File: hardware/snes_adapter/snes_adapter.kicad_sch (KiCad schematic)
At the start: 5 parts, among them J1 CART SLOT TOP ROW, J2 CART SLOT BOTTOM ROW, J3 SNES_Slot, U1 PIC12F629-IP

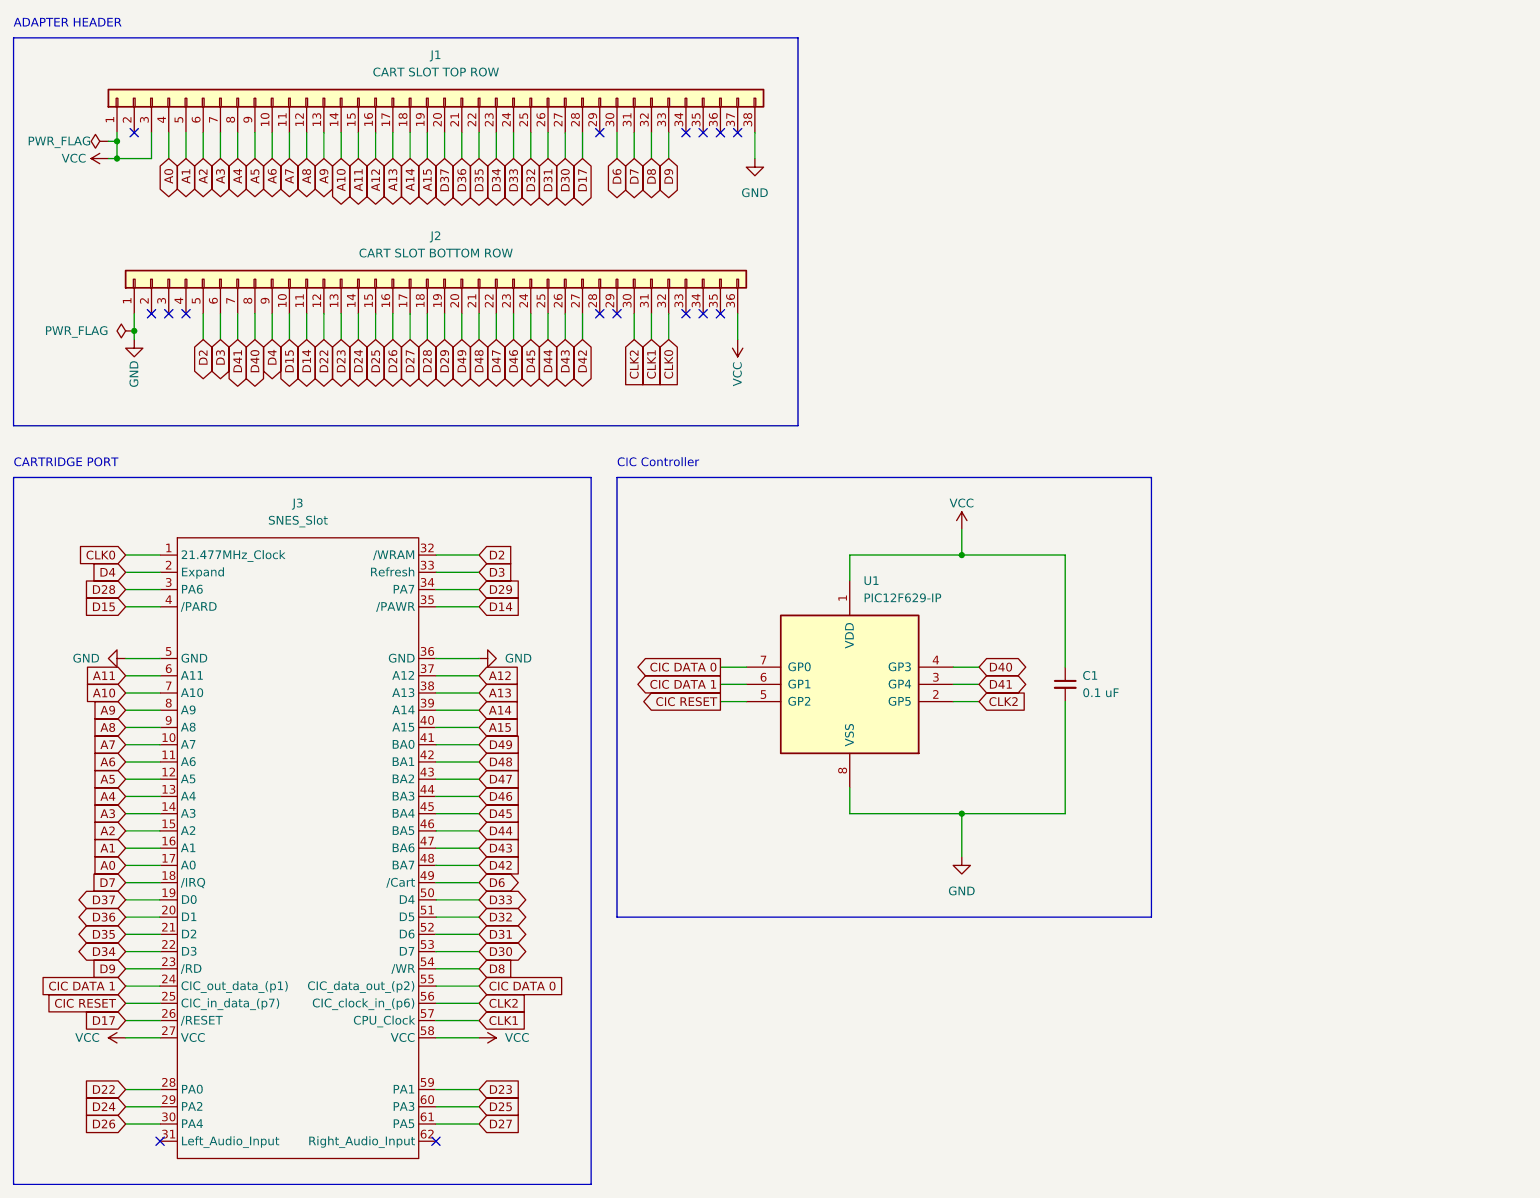
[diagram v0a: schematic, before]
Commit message: move SNES updates to clean branch
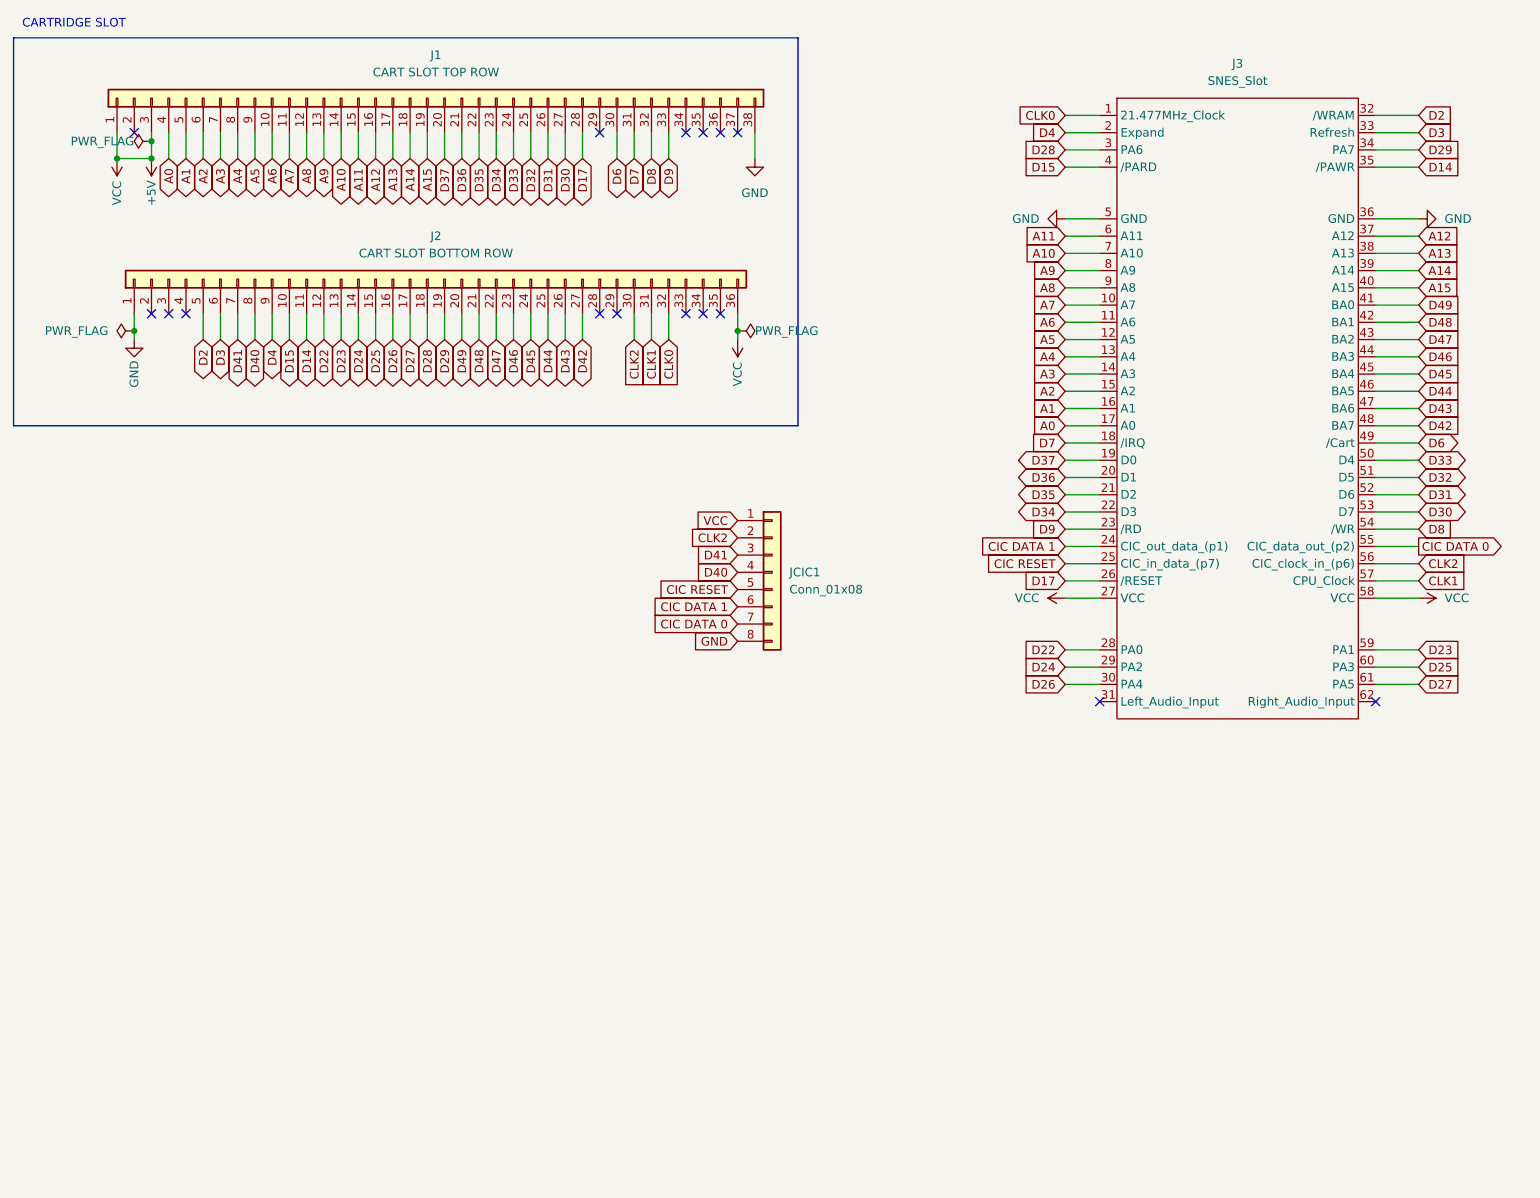
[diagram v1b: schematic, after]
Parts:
- removed C1: 0.1 uF, Capacitor_THT:C_Disc_D5.0mm_W2.5mm_P5.00mm, symbol Device:C_Small
- removed U1: PIC12F629-IP, Package_DIP:DIP-8_W7.62mm, symbol MCU_Microchip_PIC12:PIC12F629-IP
- added JCIC1: Conn_01x08, symbol Connector_Generic:Conn_01x08
- J1: footprint Connector_PinHeader_2.54mm:PinHeader_1x38_P2.54mm_Vertical -> Connector_PinSocket_2.54mm:PinSocket_1x38_P2.54mm_Vertical
- J2: footprint Connector_PinHeader_2.54mm:PinHeader_1x36_P2.54mm_Vertical -> Connector_PinSocket_2.54mm:PinSocket_1x36_P2.54mm_Vertical
- J3: footprint !OSCR:SNES Slot -> (none); symbol !OSCR:SNES_Slot -> sanni:SNES_Slot
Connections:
- net CIC DATA 0: now also JCIC1.7 (Pin_7)
- net CIC DATA 1: now also JCIC1.6 (Pin_6)
- net CIC RESET: now also JCIC1.5 (Pin_5)
- net CLK2: now also JCIC1.2 (Pin_2)
- net D40: now also JCIC1.4 (Pin_4)
- net D41: now also JCIC1.3 (Pin_3)
- net GND: now also JCIC1.8 (Pin_8)
- net VCC renamed +5V
- net +5V: now also JCIC1.1 (Pin_1)
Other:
- note added: "CARTRIDGE SLOT"
- note removed: "ADAPTER HEADER"
- note removed: "CARTRIDGE PORT"
- note removed: "CIC Controller"
- title: OSCR SHIELD - SNES BREAKOUT -> OSCR SNES ADAPTER
- moved on the sheet: J3

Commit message: Move SNES updates to clean branch
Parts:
- removed JCIC1: Conn_01x08, symbol Connector_Generic:Conn_01x08
- added C1: 0.1 uF, Capacitor_THT:C_Disc_D5.0mm_W2.5mm_P5.00mm, symbol Device:C_Small
- added U1: PIC12F629-IP, Package_DIP:DIP-8_W7.62mm, symbol MCU_Microchip_PIC12:PIC12F629-IP
- J1: footprint Connector_PinSocket_2.54mm:PinSocket_1x38_P2.54mm_Vertical -> Connector_PinHeader_2.54mm:PinHeader_1x38_P2.54mm_Vertical
- J2: footprint Connector_PinSocket_2.54mm:PinSocket_1x36_P2.54mm_Vertical -> Connector_PinHeader_2.54mm:PinHeader_1x36_P2.54mm_Vertical
- J3: footprint (none) -> !OSCR:SNES Slot; symbol sanni:SNES_Slot -> !OSCR:SNES_Slot
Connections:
- net CIC DATA 0: now also U1.7 (GP0)
- net CIC DATA 1: now also U1.6 (GP1)
- net CIC RESET: now also U1.5 (GP2)
- net CLK2: now also U1.2 (GP5)
- net D40: now also U1.4 (GP3)
- net D41: now also U1.3 (GP4)
- net GND: now also C1.2, U1.8 (VSS)
- net +5V renamed VCC
- net VCC: now also C1.1, U1.1 (VDD)
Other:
- note added: "ADAPTER HEADER"
- note added: "CARTRIDGE PORT"
- note added: "CIC Controller"
- note removed: "CARTRIDGE SLOT"
- title: OSCR SNES ADAPTER -> OSCR SHIELD - SNES BREAKOUT
- moved on the sheet: J3
